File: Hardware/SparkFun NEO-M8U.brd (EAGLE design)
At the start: 40.6 x 33 mm, 97 parts, among them J13 U.FL, J2 Qwiic Right Angle, J4 Qwiic Right Angle, U2 3.3V

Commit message: Rolls version to v10 and updates all of the parts' packages
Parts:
- J3: device SparkFun-Connectors:USB-C-16P -> SparkFun-Connectors:USB-C-16P-2LAYER-PADS
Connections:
- net SHIELD: no longer J3.SHLD5, J3.SHLD6, J3.SHLD7, J3.SHLD8
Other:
- board text added: "v10"
- board text removed: "v01"
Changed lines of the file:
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@@
 <?xml version="1.0" encoding="utf-8"?>
 <!DOCTYPE eagle SYSTEM "eagle.dtd">
-<eagle version="9.5.1">
+<eagle version="9.5.2">
 <drawing>
 <settings>
@@
 <wire x1="40.64" y1="32.9946" x2="40.64" y2="0" width="0.2032" layer="20"/>
 <wire x1="40.64" y1="0" x2="0" y2="0" width="0.2032" layer="20"/>
-<text x="34.417" y="1.27" size="1.016" layer="16" font="vector" ratio="15" rot="MR180" align="center">v01</text>
+<text x="34.417" y="1.27" size="1.016" layer="16" font="vector" ratio="15" rot="MR180" align="center">v10</text>
 <text x="-2.54" y="-8.89" size="1.778" layer="47">Measurements in inches</text>
 <dimension x1="0" y1="0" x2="0" y2="33.02" x3="-7.62" y3="16.51" textsize="1.778" textratio="15" layer="47" unit="inch"/>
@@
 <attribute name="VALUE" x="22.86" y="-0.762" size="0.6096" layer="27" font="vector" ratio="20"/>
 </element>
-<element name="J3" library="SparkFun-Connectors" package="USB-C-16P" value="" x="10.5156" y="26.8478" smashed="yes" rot="R180">
+<element name="J3" library="SparkFun-Connectors" package="USB-C-16P-2LAYER-PADS" value="" x="10.5156" y="26.8478" smashed="yes" rot="R180">
 <attribute name="NAME" x="10.5156" y="29.3878" size="0.762" layer="25" rot="R180" align="center"/>
 <attribute name="PROD_ID" value="CONN-14122" x="10.5156" y="26.8478" size="1.778" layer="27" font="vector" ratio="15" rot="R180" display="off"/>
@@
 <wire x1="29.972" y1="8.2296" x2="30.607" y2="8.864603125" width="0.508" layer="16"/>
 <via x="30.607" y="11.8872" extent="1-16" drill="0.3048"/>
-<wire x1="30.607" y1="8.864603125" x2="30.607" y2="11.684" width="0.508" layer="16"/>
+<wire x1="30.607" y1="8.864603125" x2="30.607" y2="11.8872" width="0.508" layer="16"/>
 <wire x1="30.607" y1="11.8872" x2="30.607" y2="14.4526" width="0.508" layer="1"/>
 <wire x1="25.0063" y1="4.8133" x2="25.019" y2="4.8006" width="0.508" layer="1"/>
@@
 <wire x1="26.2636" y1="6.0706" x2="25.0063" y2="4.8133" width="0.508" layer="1"/>
 <wire x1="26.2636" y1="6.0706" x2="29.9212" y2="6.0706" width="0.508" layer="1"/>
-<wire x1="34.544" y1="11.9126" x2="34.3154" y2="11.684" width="0.1524" layer="16"/>
-<wire x1="34.3154" y1="11.684" x2="30.607" y2="11.684" width="0.1524" layer="16"/>
 <wire x1="30.607" y1="14.4526" x2="30.16" y2="14.8996" width="0.508" layer="1"/>
 <wire x1="29.8149" y1="14.8996" x2="30.16" y2="14.8996" width="0.508" layer="1"/>
-<wire x1="30.607" y1="11.684" x2="30.607" y2="11.8872" width="0.508" layer="16"/>
 <wire x1="5.08" y1="22.5806" x2="5.08" y2="20.574" width="0.508" layer="16"/>
 <wire x1="5.08" y1="20.574" x2="5.08" y2="18.0006" width="0.508" layer="16"/>
@@
 <wire x1="13.3024" y1="10.483" x2="14.32" y2="10.483" width="0.508" layer="1"/>
 <wire x1="12.7" y1="6.0706" x2="12.7" y2="6.9986" width="0.508" layer="1"/>
+<wire x1="34.5313" y1="11.9126" x2="30.6324" y2="11.9126" width="0.1524" layer="16"/>
+<wire x1="30.6324" y1="11.9126" x2="30.607" y2="11.8872" width="0.508" layer="16"/>
 </signal>
 <signal name="GND">
@@
 <contactref element="PPS" pad="2"/>
 <via x="27.686" y="11.4046" extent="1-16" drill="0.3048"/>
-<wire x1="34.0106" y1="10.1346" x2="33.02" y2="10.1346" width="0.1524" layer="16"/>
+<wire x1="33.02" y1="10.1346" x2="34.0106" y2="10.1346" width="0.1524" layer="16"/>
 <via x="33.02" y="10.1346" extent="1-16" drill="0.3048"/>
-<wire x1="34.544" y1="9.6012" x2="34.0106" y2="10.1346" width="0.1524" layer="16"/>
 <wire x1="32.0548" y1="9.1694" x2="33.02" y2="10.1346" width="0.1524" layer="1"/>
 <via x="32.239884375" y="4.869515625" extent="1-16" drill="0.3048"/>
@@
 <wire x1="13.97" y1="1.27" x2="17.145" y2="4.445" width="0.17" layer="16"/>
 <wire x1="17.145" y1="4.445" x2="26.8801125" y2="4.445" width="0.17" layer="16"/>
+<wire x1="34.0106" y1="10.1346" x2="34.5313" y2="9.6139" width="0.1524" layer="16"/>
+<wire x1="34.5313" y1="9.6139" x2="34.5313" y2="9.6012" width="0.1524" layer="16"/>
 </signal>
 <signal name="N$5">
@@
 <wire x1="4.2164" y1="23.6846" x2="4.191" y2="23.71" width="0.1524" layer="1"/>
 <via x="4.191" y="24.765" extent="1-16" drill="0.3048"/>
-<wire x1="4.191" y1="24.765" x2="4.445" y2="24.765" width="0.1524" layer="16"/>
-<wire x1="4.445" y1="24.765" x2="6.096" y2="23.114" width="0.1524" layer="16"/>
-<wire x1="6.096" y1="23.114" x2="6.096" y2="22.5806" width="0.1524" layer="16"/>
+<wire x1="4.191" y1="24.765" x2="4.953" y2="24.765" width="0.1524" layer="16"/>
+<wire x1="6.1214" y1="23.5966" x2="6.1214" y2="22.5806" width="0.1524" layer="16"/>
+<wire x1="4.953" y1="24.765" x2="6.1214" y2="23.5966" width="0.1524" layer="16"/>
 </signal>
 <signal name="N$8">
@@
 <wire x1="2.5908" y1="23.6846" x2="2.54" y2="23.7354" width="0.1524" layer="1"/>
 <via x="2.54" y="24.765" extent="1-16" drill="0.3048"/>
-<wire x1="2.54" y1="24.765" x2="2.667" y2="24.765" width="0.1524" layer="16"/>
-<wire x1="2.667" y1="24.765" x2="4.064" y2="23.368" width="0.1524" layer="16"/>
-<wire x1="4.064" y1="23.368" x2="4.064" y2="22.5806" width="0.1524" layer="16"/>
+<wire x1="4.0386" y1="23.5204" x2="4.0386" y2="22.5806" width="0.1524" layer="16"/>
+<wire x1="2.794" y1="24.765" x2="4.0386" y2="23.5204" width="0.1524" layer="16"/>
+<wire x1="2.54" y1="24.765" x2="2.794" y2="24.765" width="0.1524" layer="16"/>
 </signal>
 <signal name="N$2">
@@
 <contactref element="R11" pad="2"/>
 <wire x1="38.1" y1="9.3726" x2="37.8714" y2="9.6012" width="0.1524" layer="16"/>
-<wire x1="37.8714" y1="9.6012" x2="35.56" y2="9.6012" width="0.1524" layer="16"/>
+<wire x1="37.8714" y1="9.6012" x2="35.5727" y2="9.6012" width="0.1524" layer="16"/>
 <via x="38.1" y="9.3726" extent="1-16" drill="0.3048"/>
 <wire x1="38.95" y1="10.3124" x2="38.95" y2="10.2226" width="0.1524" layer="1"/>
@@
 <vertex x="5.969" y="33.02"/>
 </polygon>
-<contactref element="J3" pad="SHLD7"/>
-<contactref element="J3" pad="SHLD6"/>
 <contactref element="J3" pad="SHLD4"/>
 <contactref element="J3" pad="SHLD1"/>
-<contactref element="J3" pad="SHLD5"/>
 <contactref element="J3" pad="SHLD2"/>
 <contactref element="J3" pad="SHLD3"/>
-<contactref element="J3" pad="SHLD8"/>
 <via x="8.5598" y="30.4546" extent="1-16" drill="0.381"/>
 <via x="12.7" y="30.48" extent="1-16" drill="0.381"/>
@@
 <contactref element="PWR\" pad="1"/>
 <contactref element="R1" pad="2"/>
-<wire x1="36.2712" y1="11.938" x2="35.5854" y2="11.938" width="0.1524" layer="16"/>
-<wire x1="35.5854" y1="11.938" x2="35.56" y2="11.9126" width="0.1524" layer="16"/>
 <via x="36.2712" y="11.938" extent="1-16" drill="0.3048"/>
 <wire x1="37.25" y1="11.8364" x2="36.3728" y2="11.8364" width="0.1524" layer="1"/>
 <wire x1="36.3728" y1="11.8364" x2="36.2712" y2="11.938" width="0.1524" layer="1"/>
+<wire x1="36.2712" y1="11.938" x2="36.2458" y2="11.9126" width="0.1524" layer="16"/>
+<wire x1="36.2458" y1="11.9126" x2="35.5727" y2="11.9126" width="0.1524" layer="16"/>
 </signal>
 <signal name="N$7">

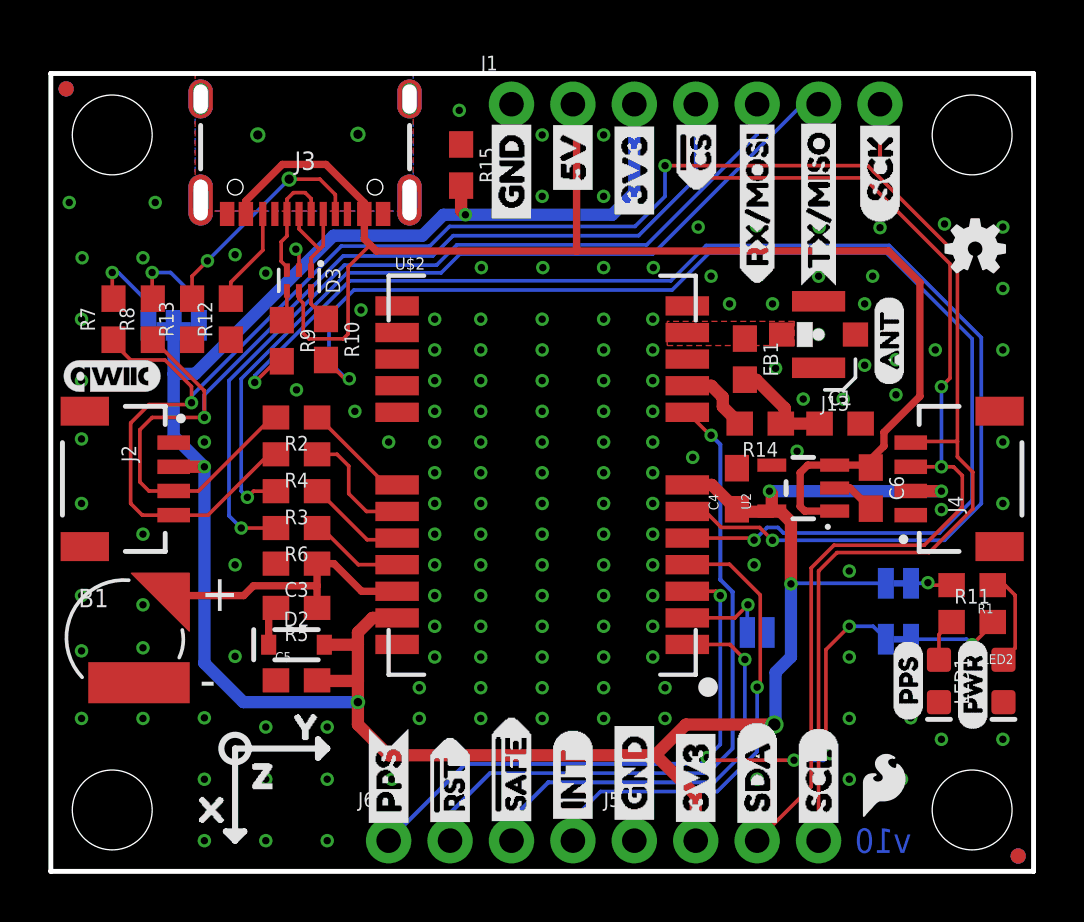
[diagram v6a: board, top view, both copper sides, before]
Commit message: Removes old gerbers and buzzard labels, fixes some minor board inconsistencies
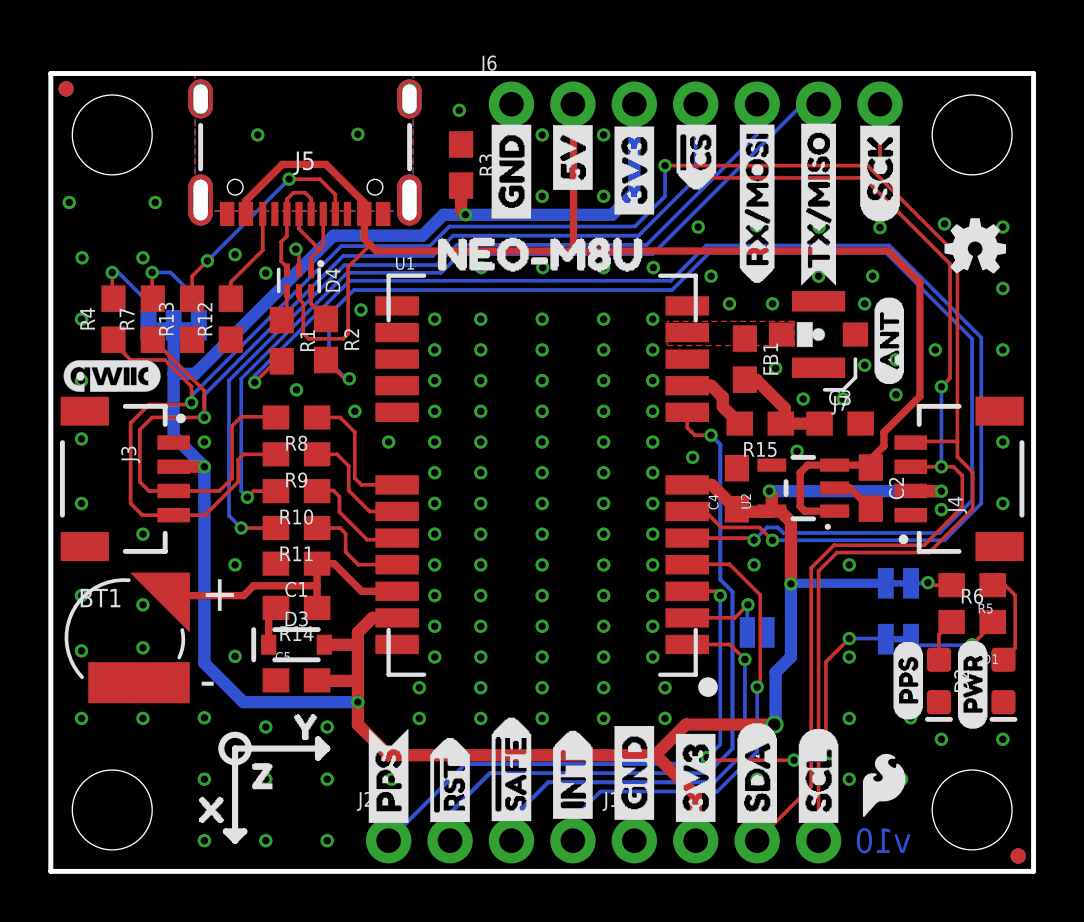
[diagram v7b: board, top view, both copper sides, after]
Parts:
- removed JP21, JP61, JP71, JP81: FIDUCIALUFIDUCIAL, SparkFun:MICRO-FIDUCIAL
- removed LED1: BLUE, SparkFun-LED:LED-0603
- added D4: PRTR5V0U2F, SparkFun-IC-Power:SOT886
- added JP1: JUMPER-SMT_3_2-NC_TRACE_SILK, SparkFun-Jumpers:SMT-JUMPER_3_2-NC_TRACE_SILK
- added JP6, JP7, JP8: FIDUCIALUFIDUCIAL, SparkFun:MICRO-FIDUCIAL
- added U1: U-BLOX_MEO-M8U, SparkFun-GPS:NEO-M9N/M8T/M8U
- C1: value 47pF -> 1.0uF
- C3: value 1.0uF -> 47pF
- D2: value 0.5A/40V/420mV -> BLUE; device SparkFun-DiscreteSemi:SOD-323 -> SparkFun-LED:LED-0603
- D3: value PRTR5V0U2F -> 0.5A/40V/420mV; device SparkFun-IC-Power:SOT886 -> SparkFun-DiscreteSemi:SOD-323
- J1: device SparkFun-Connectors:1X07_NO_SILK -> SparkFun-Connectors:1X04_NO_SILK
- J2: value Qwiic Right Angle -> (none); device SparkFun-Connectors:JST04_1MM_RA -> SparkFun-Connectors:1X04_NO_SILK
- J3: value (none) -> Qwiic Right Angle; device SparkFun-Connectors:USB-C-16P-2LAYER-PADS -> SparkFun-Connectors:JST04_1MM_RA
- J5: device SparkFun-Connectors:1X04_NO_SILK -> SparkFun-Connectors:USB-C-16P-2LAYER-PADS
- J6: device SparkFun-Connectors:1X04_NO_SILK -> SparkFun-Connectors:1X07_NO_SILK
- JP5: value JUMPER-SMT_3_2-NC_TRACE_SILK -> FIDUCIALUFIDUCIAL; device SparkFun-Jumpers:SMT-JUMPER_3_2-NC_TRACE_SILK -> SparkFun:MICRO-FIDUCIAL
- R1: value 1k -> 27
- R10, R9: value 27 -> 33
- R11: value 1k -> 33
- R14: value 10 -> 1k
- R15: value 100k -> 10
- R2: value 33 -> 27
- R3: value 33 -> 100k
- R4: value 33 -> 2.2k
- R6: value 33 -> 1k
- R8: value 2.2k -> 33
- U$2: value U-BLOX_MEO-M8U -> (none); device SparkFun-GPS:NEO-M9N/M8T/M8U -> interrupt:INT1
- U$34: device interrupt:INT0 -> buzzard_labels:NEO#M8U0
- moved JP5 41.2 mm to (40.0, 0.64), flipped to the top
- moved J1 30.9 mm to (24.1, 1.27)
- moved J6 30.9 mm to (19.1, 31.7)
- moved R1 30.3 mm to (9.55, 21.9), turned to 270 degrees
- moved J5 29.0 mm to (10.5, 26.8), turned to 180 degrees
- moved R11 28.2 mm to (10.2, 14.2), turned to 180 degrees
- moved R6 28.2 mm to (38.1, 10.3), turned to 0 degrees
- moved R5 28.0 mm to (38.1, 11.8)
- moved D2 26.6 mm to (36.7, 7.87), turned to 270 degrees
- moved U$34 24.8 mm to (14.9, 25.5), flipped to the top, turned to 0 degrees
- moved C1 23.2 mm to (10.2, 12.7), turned to 180 degrees
- moved C3 23.2 mm to (32.6, 18.5), turned to 0 degrees
- moved R14 20.6 mm to (10.2, 10.9)
- moved J2 17.4 mm to (14.0, 1.27), turned to 0 degrees
- moved R15 16.4 mm to (29.3, 18.5), turned to 180 degrees
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- renumbered B1 to BT1, C6 to C2, J13 to J7, JP101 to JP10, JP31 to JP11, JP41 to JP12, JP91 to JP9, LED2 to D1, PPS to JP3, PWR\ to JP2, SPI to JP4
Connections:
- net !RESET: now also J2.2, U1.8; no longer J6.2, U$2.8
- net 3.3V: now also D3.A, J1.2, J3.2, J6.3, JP1.2, R3.2, U1.23, U1.7; no longer D2.A, J1.3, J2.2, J5.2, JP5.2, R15.2, U$2.23, U$2.7
- net 5V: now also D4.5, J5.VBUS1, J5.VBUS2, J6.2; no longer D3.5, J1.2, J3.VBUS1, J3.VBUS2
- net ANT_VCC: now also C3.1, R15.1; no longer C1.1, R14.1
- net D+: now also D4.4, R1.1; no longer D3.4, R9.1
- net D-: now also D4.6, R2.1; no longer D3.6, R10.1
- net D_SEL: now also U1.2; no longer U$2.2
- net EXT_INT: now also J2.4, U1.4; no longer J6.4, U$2.4
- net GND: now also D2.C, D4.2, J3.1, J5.GND, J5.GND2, J6.1, R3.1, U1.10, U1.12, U1.13, U1.24; no longer D3.2, J2.1, J3.GND, J3.GND2, J5.1, LED1.C, R15.1, U$2.10, U$2.12, U$2.13, U$2.24
- net GPS_ANT1: now also U1.11; no longer U$2.11
- net N$1: now also R5.2; no longer R1.2
- net N$10: now also R5.1; no longer R1.1
- net N$11: now also R1.2, U1.6; no longer R9.2, U$2.6
- net N$12: now also R2.2, U1.5; no longer R10.2, U$2.5
- net N$13: now also R9.1, U1.19; no longer R4.1, U$2.19
- net N$15: now also R10.1, U1.20; no longer R3.1, U$2.20
- net N$16: now also R11.1, U1.21; no longer R6.1, U$2.21
- net N$2: now also D2.A, R6.1; no longer LED1.A, R11.1
- net N$3: now also R8.1, U1.18; no longer R2.1, U$2.18
- net N$4: now also R6.2; no longer R11.2
- net N$5: now also JP1.1, R7.2; no longer JP5.1, R8.2
- net N$6: now also D3.C, R14.2; no longer D2.C, R5.2
- net N$7: now also J5.B5; no longer J3.B5
- net N$8: now also JP1.3, R4.2; no longer JP5.3, R7.2
- net N$9: now also J5.A5; no longer J3.A5
- net PPS: now also J2.1, U1.3; no longer J6.1, U$2.3
- net RXI/MOSI: now also J6.5, R11.2; no longer J1.5, R6.2
- net SCL/SCK: now also J1.4, J3.4, J6.7, R4.1, R9.2; no longer J1.7, J2.4, J5.4, R4.2, R7.1
- net SDA/!CS: now also J1.3, J3.3, J6.4, R7.1, R8.2; no longer J1.4, J2.3, J5.3, R2.2, R8.1
- net SHIELD: now also J5.SHLD1, J5.SHLD2, J5.SHLD3, J5.SHLD4; no longer J3.SHLD1, J3.SHLD2, J3.SHLD3, J3.SHLD4
- net TP2/!SAFE: now also J2.3, U1.1; no longer J6.3, U$2.1
- net TXO/MISO: now also J6.6, R10.2; no longer J1.6, R3.2
- net USB_D+: now also D4.3, J5.A6, J5.B6; no longer D3.3, J3.A6, J3.B6
- net USB_D-: now also D4.1, J5.A7, J5.B7; no longer D3.1, J3.A7, J3.B7
- net VDD: now also R15.2, U1.9; no longer R14.2, U$2.9
- net V_BATT: now also C1.1, R14.1, U1.22; no longer C3.1, R5.1, U$2.22
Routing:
- net N$3: track 4.46 -> 6.04 mm
- net SDA/!CS: track 87.8 -> 89.1 mm
- net PPS: track 35.7 -> 35.0 mm
- net N$15: track 4.17 -> 4.77 mm
- net SCL/SCK: track 90.6 -> 91.1 mm

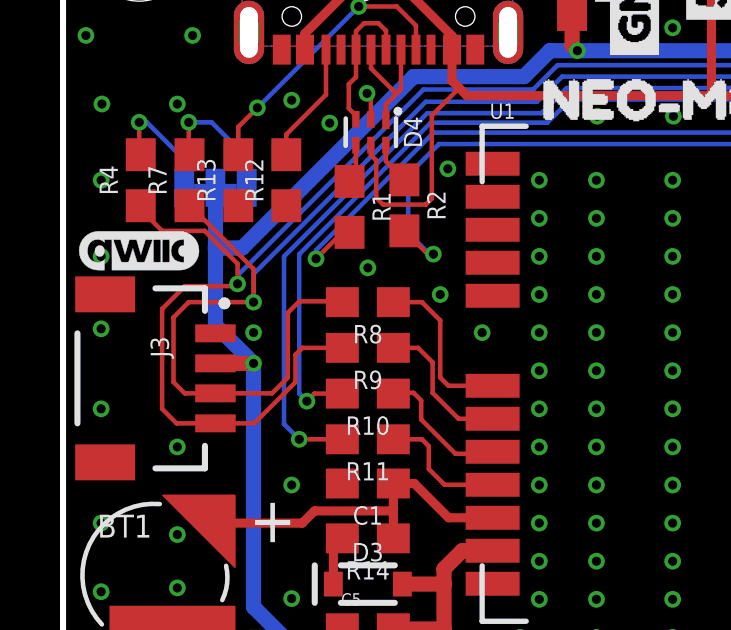
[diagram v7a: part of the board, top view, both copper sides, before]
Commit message: Updates some silk, removes wire stubs
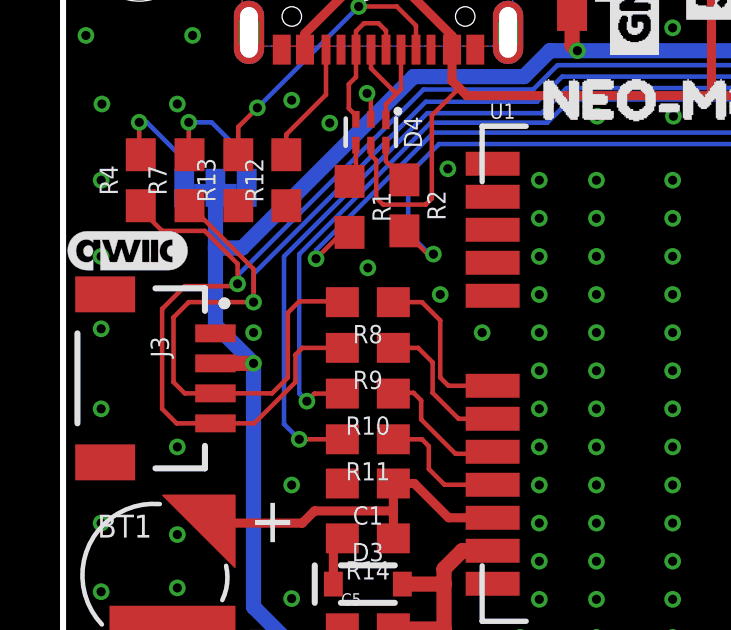
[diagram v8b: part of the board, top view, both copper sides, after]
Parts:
- moved U$14 0.38 mm to (2.16, 20.5)
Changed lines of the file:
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@@
 </element>
 <element name="U$11" library="board lables" package="SPI1" value="" x="30.607" y="11.684" smashed="yes" rot="MR0"/>
-<element name="U$14" library="SparkFun-Aesthetics" package="QWIIC_4MM" value="" x="2.54" y="20.4724" smashed="yes"/>
+<element name="U$14" library="SparkFun-Aesthetics" package="QWIIC_4MM" value="" x="2.159" y="20.4724" smashed="yes"/>
 <element name="U$12" library="LEDs" package="PPS0" value="" x="36.703" y="7.747" smashed="yes" rot="MR0"/>
 <element name="U$17" library="LEDs" package="PWR1" value="" x="36.957" y="13.716" smashed="yes" rot="MR0"/>
@@
 <contactref element="U1" pad="18"/>
 <contactref element="R8" pad="1"/>
-<wire x1="13.862" y1="15.983" x2="14.32" y2="15.983" width="0.1524" layer="1"/>
 <wire x1="14.32" y1="15.983" x2="12.846" y2="15.983" width="0.1524" layer="1"/>
 <wire x1="12.573" y1="16.256" x2="12.573" y2="18.161" width="0.1524" layer="1"/>
@@
 <contactref element="R10" pad="1"/>
 <wire x1="11.01" y1="15.7226" x2="11.0168" y2="15.7158" width="0.1524" layer="1"/>
-<wire x1="11.0168" y1="15.7158" x2="11.1116" y2="15.621" width="0.1524" layer="1"/>
-<wire x1="11.1116" y1="15.621" x2="11.176" y2="15.621" width="0.1524" layer="1"/>
 <wire x1="14.32" y1="13.783" x2="14.253" y2="13.716" width="0.1524" layer="1"/>
 <wire x1="11.938" y1="15.494" x2="11.684" y2="15.748" width="0.1524" layer="1"/>
